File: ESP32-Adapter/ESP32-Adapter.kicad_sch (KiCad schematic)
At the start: 0 parts

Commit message: complete adapter board schem
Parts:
- added C1: 0.1µ, symbol Device:C
- added C2: 1µ, symbol Device:C
- added D1: D, symbol Device:D
- added J1, J4, J5, J6, J7, J8, J9: Conn_01x01_Socket, symbol Connector:Conn_01x01_Socket
- added J12, J13: Conn_01x05, symbol Connector_Generic:Conn_01x05
- added J14: Conn_01x04, symbol Connector_Generic:Conn_01x04
- added J2, J3: Conn_01x03, symbol Connector_Generic:Conn_01x03
- added R1: 820, symbol Device:R
- added R2: 270, symbol Device:R
- added U1: ESP32-C5-DevKitC-1, PCM_Espressif:ESP32-C5-DevKitC-1, symbol PCM_Espressif:ESP32-C5-DevKitC-1
- added U2: LM317_TO-263, Package_TO_SOT_SMD:TO-263-2, symbol Regulator_Linear:LM317_TO-263
- added U3: Adafruit CANPAL, symbol Interface_CAN_LIN:CANPAL
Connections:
- new net: J3.1 (Pin_1), J5.1 (Pin_1)
- new net: J14.2 (Pin_2), U1.11 (GPIO7)
- new net: J14.3 (Pin_3), U1.10 (GPIO6)
- new net: J14.4 (Pin_4), J6.1 (Pin_1), J8.1 (Pin_1), U1.1 (3V3)
- new net: C2.1, D1.2 (A), U2.2 (VO)
- new net: C1.1, J1.1 (Pin_1), R2.2, U2.3 (VI)
- new net: J12.1 (Pin_1), U1.4 (GPIO3/MTDI)
- new net: J12.2 (Pin_2), U1.28 (GPIO23)
- new net: J12.3 (Pin_3), U1.25 (GPIO9)
- new net: D1.1 (K), J12.5 (Pin_5), J13.5 (Pin_5), J7.1 (Pin_1), J9.1 (Pin_1), U1.14 (5V), U3. (CANL)
- new net: J3.2 (Pin_2), U1.3 (GPIO2/MTMS)
- new net: R1.2, U2.1 (ADJ)
- new net: J13.1 (Pin_1), U1.29 (GPIO24)
- new net: J13.2 (Pin_2), U1.26 (GPIO10)
- new net: J13.3 (Pin_3), U1.24 (GPIO8)
- new net: U1.5 (GPIO4/MTCK), U3. (CANL)
- new net: U1.6 (GPIO5/MTDO), U3. (CANL)
- new net: J2.2 (Pin_2), U1.8 (GPIO1)
- new net: J2.1 (Pin_1), J4.1 (Pin_1)
- new net GND: C1.2, C2.2, J12.4 (Pin_4), J13.4 (Pin_4), J14.1 (Pin_1), J2.3 (Pin_3), J3.3 (Pin_3), R1.1, R2.1, U1.15 (GND), U1.18 (GND), U1.21 (GND), U1.32 (GND), U3. (CANL)
- no-connect marks 0 -> 13
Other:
- note added: "3.3V"
- note added: "5V"
- note added: "A1"
- note added: "A2"
- note added: "Analog 1"
- note added: "Analog 2"
- note added: "B1"
- note added: "B2"
- note added: "CAN RX"
- note added: "CAN TX"
- note added: "Encoder 1"
- note added: "Encoder 2"
- note added: "GND"
- note added: "I2C"
- note added: "IDX1"
- note added: "IDX2"
- note added: "MILLIONS NERVES"
- note added: "SCL"
- note added: "SDA"
- note added: "SIG1"
- note added: "SIG2"
- note added: "V-in from PDP"
- note added: "Vcc"
- note added: "vash the stampede"

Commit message: create pcb
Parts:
- removed J1, J4, J5, J6, J7, J8, J9: Conn_01x01_Socket, symbol Connector:Conn_01x01_Socket
- added J1: Conn_01x08_Pin, Connector_PinHeader_2.54mm:PinHeader_2x04_P2.54mm_Vertical, symbol Connector:Conn_01x08_Pin
- added J10: Barrel_Jack, Connector_BarrelJack:BarrelJack_CUI_PJ-063AH_Horizontal, symbol Connector:Barrel_Jack
- C1, C2: footprint (none) -> Capacitor_SMD:C_0402_1005Metric
- D1: footprint (none) -> Diode_SMD:D_0805_2012Metric
- J12, J13: footprint (none) -> Connector_JST:JST_XH_S5B-XH-A-1_1x05_P2.50mm_Horizontal
- J14: footprint (none) -> Connector_JST:JST_XH_S4B-XH-A-1_1x04_P2.50mm_Horizontal
- J2, J3: footprint (none) -> Connector_JST:JST_XH_S3B-XH-A-1_1x03_P2.50mm_Horizontal
- R1, R2: footprint (none) -> Resistor_SMD:R_0402_1005Metric
- U3: footprint (none) -> Audio_Module:canpal
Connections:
- net GND: now also J12.1 (Pin_1), J13.1 (Pin_1), J14.4 (Pin_4), U3.2 (GND), J10.2; no longer J12.4 (Pin_4), J13.4 (Pin_4), J14.1 (Pin_1), R2.1, U3. (CANL)
- net at J3.1 (Pin_1): now also J1.6 (Pin_6), J1.8 (Pin_8)
- net I2C SCL: now reaches J14.2 (Pin_2), U1.11 (GPIO7)
- net I2C SDA: now reaches J14.3 (Pin_3), U1.10 (GPIO6)
- net +3.3V: now reaches U1.1 (3V3)
- net +3.3V: now also J14.1 (Pin_1), U3.1 (Vcc), J1.3 (Pin_3), J1.7 (Pin_7); no longer J14.4 (Pin_4)
- net at C2.1, D1.2 (A), U2.2 (VO): now also R2.2
- net at C1.1, U2.3 (VI): now also J10.1; no longer R2.2
- net B2: now reaches U1.4 (GPIO3/MTDI)
- net B2: now also J12.2 (Pin_2); no longer J12.1 (Pin_1)
- net A2: now reaches U1.28 (GPIO23)
- net A2: now also J12.3 (Pin_3); no longer J12.2 (Pin_2)
- net IDX2: now reaches U1.25 (GPIO9)
- net IDX2: now also J12.4 (Pin_4); no longer J12.3 (Pin_3)
- net +5V: now reaches D1.1 (K), J12.5 (Pin_5), J13.5 (Pin_5), U1.14 (5V)
- net +5V: now also J1.1 (Pin_1), J1.5 (Pin_5); no longer U3. (CANL)
- net SIG2: now reaches J3.2 (Pin_2), U1.3 (GPIO2/MTMS)
- net at R1.2, U2.1 (ADJ): now also R2.1
- net B1: now reaches U1.29 (GPIO24)
- net B1: now also J13.2 (Pin_2); no longer J13.1 (Pin_1)
- net A1: now reaches U1.26 (GPIO10)
- net A1: now also J13.3 (Pin_3); no longer J13.2 (Pin_2)
- net IDX1: now reaches U1.24 (GPIO8)
- net IDX1: now also J13.4 (Pin_4); no longer J13.3 (Pin_3)
- net CAN TX: now reaches U1.5 (GPIO4/MTCK)
- net CAN TX: now also U3.4 (TX); no longer U3. (CANL)
- net CAN RX: now reaches U1.6 (GPIO5/MTDO)
- net CAN RX: now also U3.3 (RX); no longer U3. (CANL)
- net SIG1: now reaches J2.2 (Pin_2), U1.8 (GPIO1)
- net at J2.1 (Pin_1): now also J1.2 (Pin_2), J1.4 (Pin_4)
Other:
- note added: "Analog"
- note added: "CANPal"
- note added: "PDP Step-Down"
- note added: "PDP-V"
- note added: "Quadrature Encoders"
- note added: "Voltage Sel"
- note removed: "3.3V"
- note removed: "5V"
- note removed: "A1"
- note removed: "A2"
- note removed: "B1"
- note removed: "B2"
- note removed: "CAN RX"
- note removed: "CAN TX"
- note removed: "GND"
- note removed: "IDX1"
- note removed: "IDX2"
- note removed: "SCL"
- note removed: "SDA"
- note removed: "SIG1"
- note removed: "SIG2"
- note removed: "V-in from PDP"
- moved on the sheet: C1, C2, D1, J12, J13, J14, J2, J3, R1, R2, U2

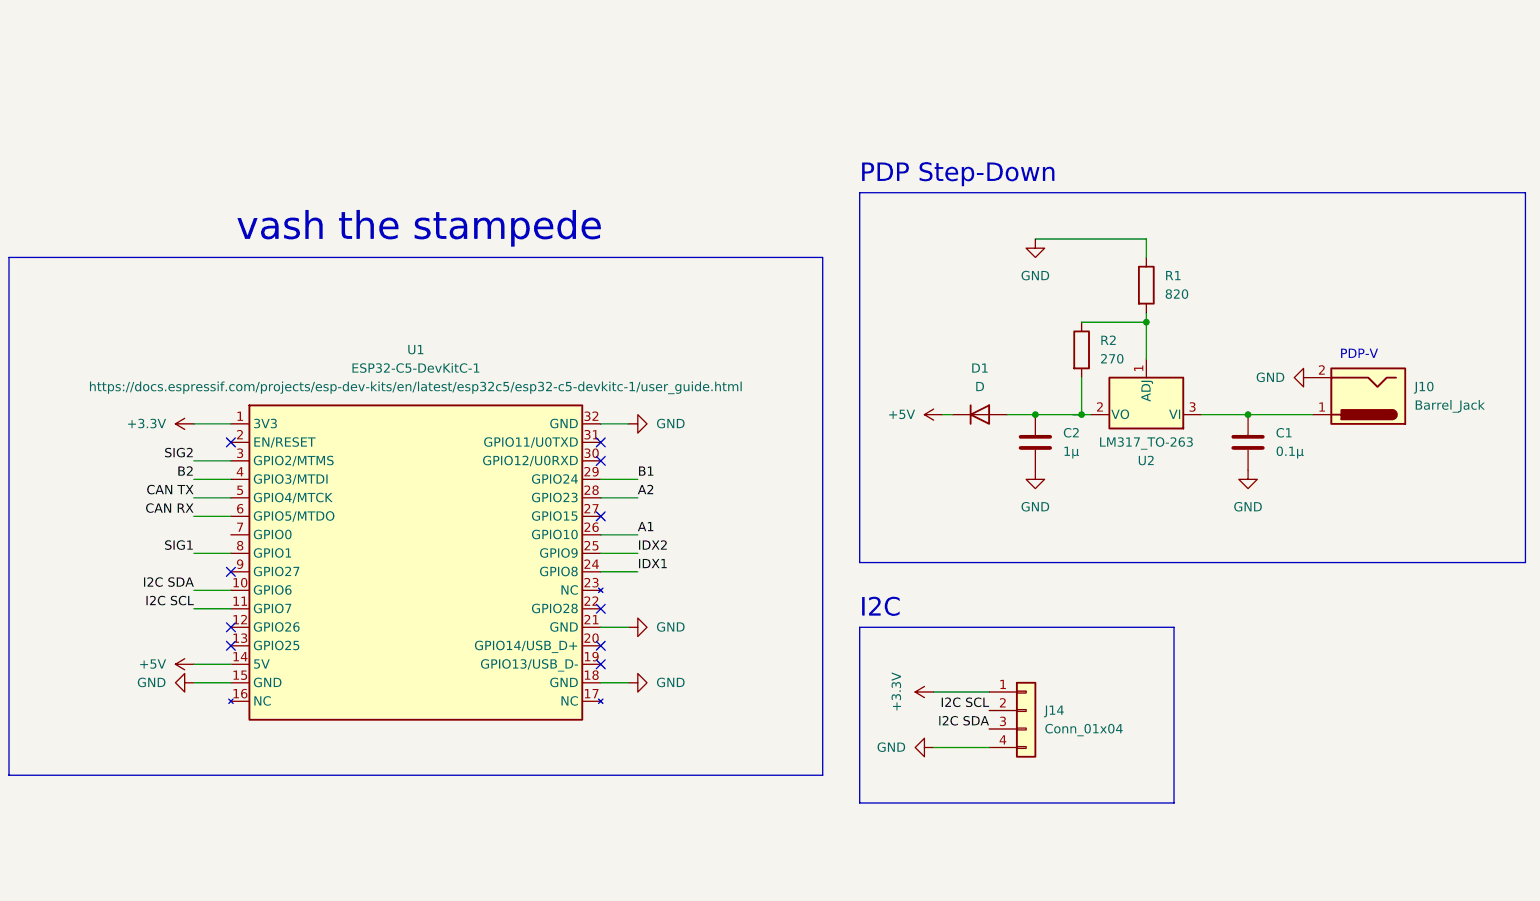
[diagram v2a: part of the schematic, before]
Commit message: finish first version of neopixel board
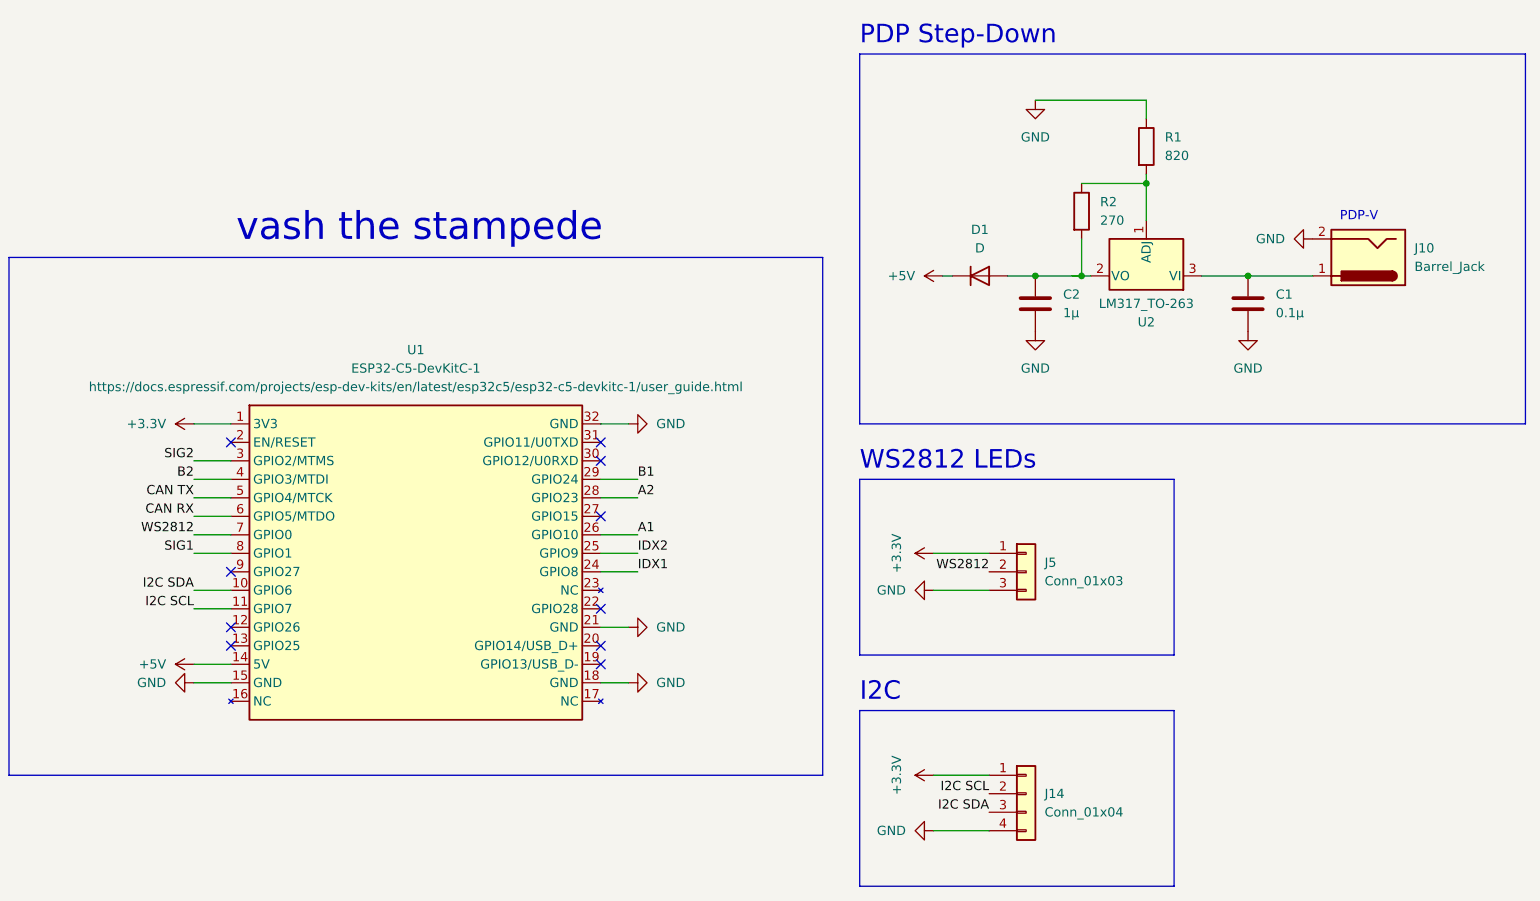
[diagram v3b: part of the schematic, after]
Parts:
- added J5: Conn_01x03, Connector_JST:JST_XH_S3B-XH-A-1_1x03_P2.50mm_Horizontal, symbol Connector_Generic:Conn_01x03
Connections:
- net +3.3V: now also J5.1 (Pin_1)
- net GND: now also J5.3 (Pin_3)
- net WS2812: now reaches U1.7 (GPIO0)
- net WS2812: now also J5.2 (Pin_2)
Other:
- note added: "WS2812 LEDs"
- moved on the sheet: C1, C2, D1, J10, J14, R1, R2, U2

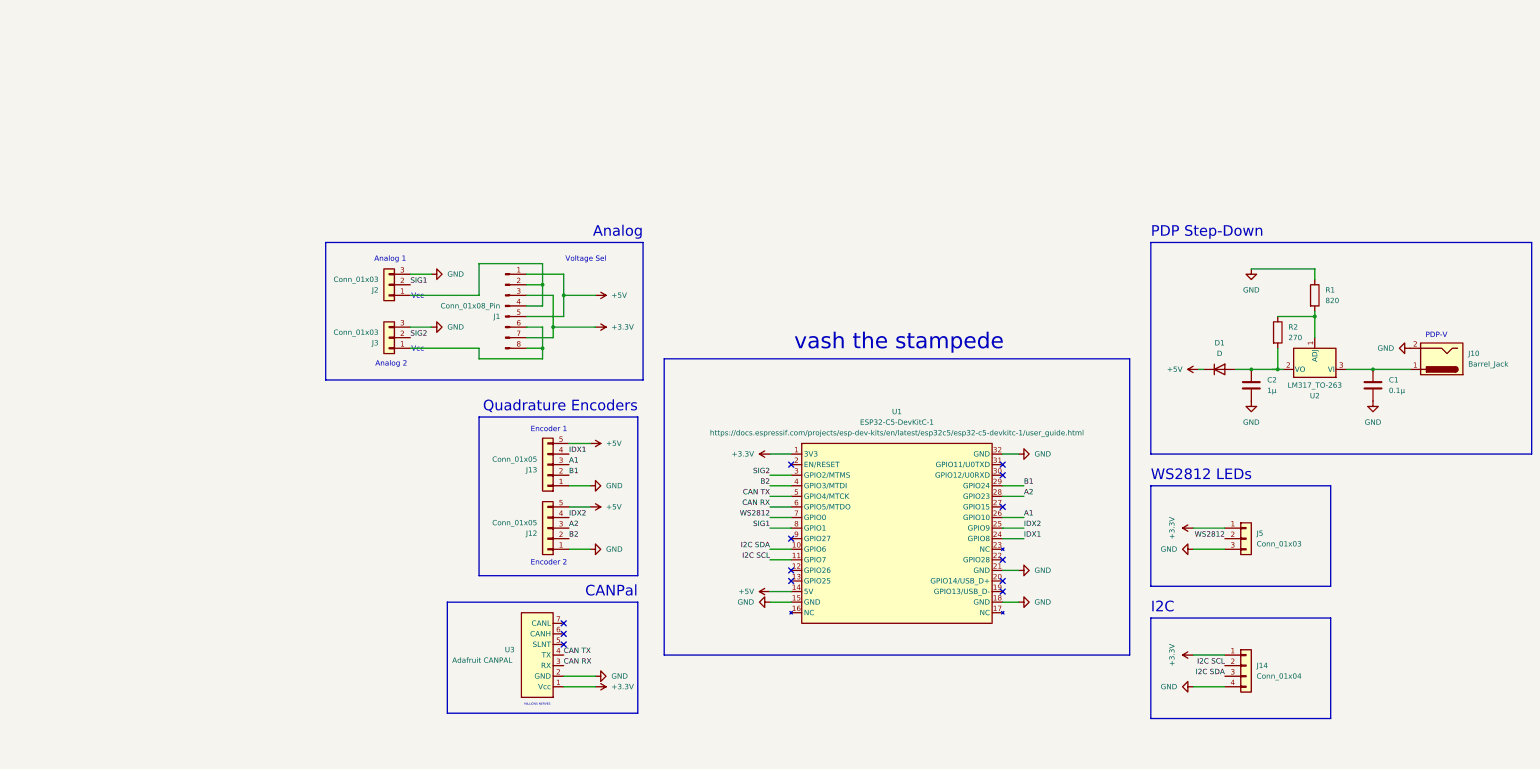
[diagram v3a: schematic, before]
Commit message: Redo board partially
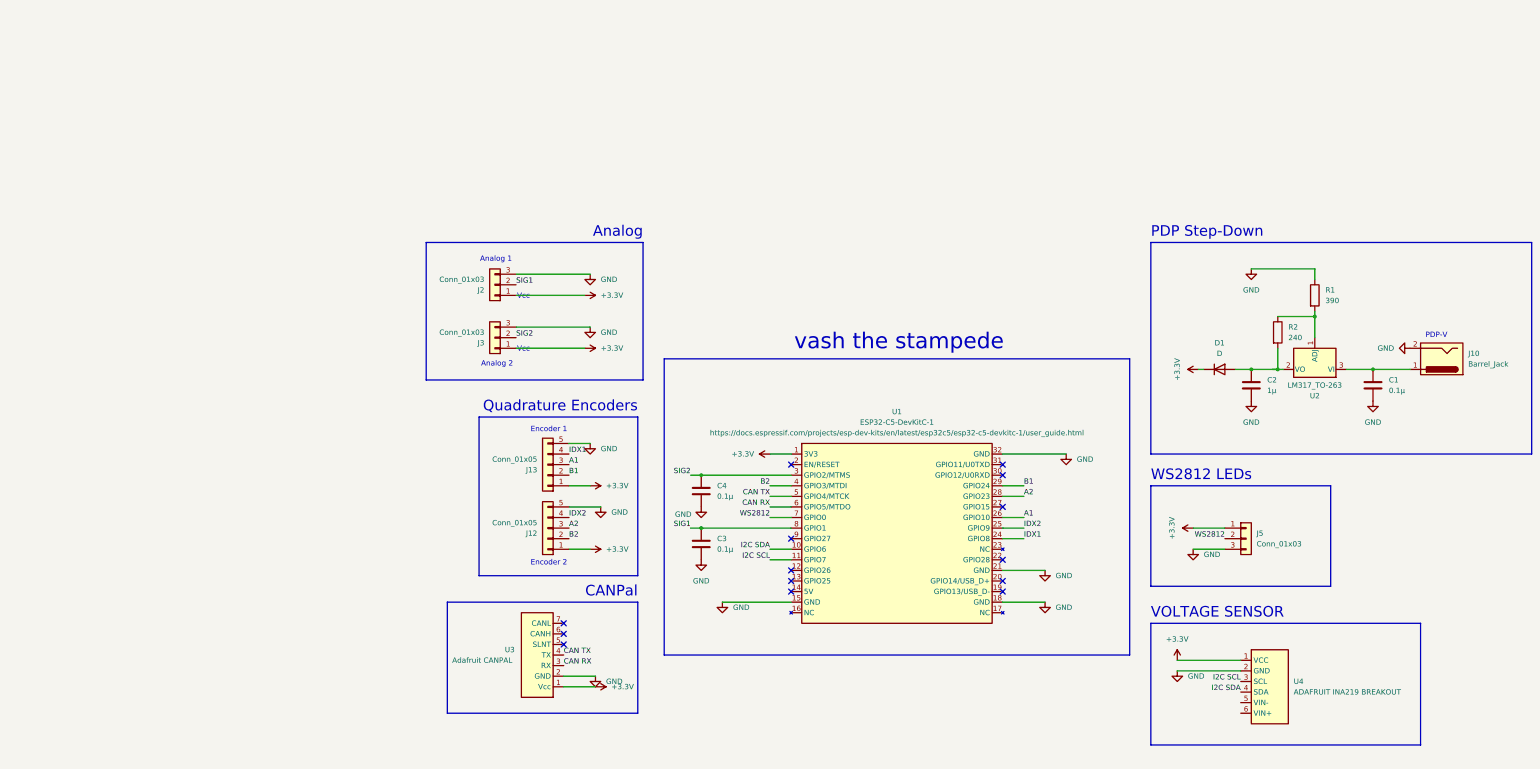
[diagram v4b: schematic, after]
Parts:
- removed J1: Conn_01x08_Pin, Connector_PinHeader_2.54mm:PinHeader_2x04_P2.54mm_Vertical, symbol Connector:Conn_01x08_Pin
- removed J14: Conn_01x04, Connector_JST:JST_XH_S4B-XH-A-1_1x04_P2.50mm_Horizontal, symbol Connector_Generic:Conn_01x04
- added C3, C4: 0.1µ, Capacitor_SMD:C_0402_1005Metric, symbol Device:C
- added U4: ADAFRUIT INA219 BREAKOUT, Audio_Module:INA219 Breakout, symbol Analog_ADC:INA219_ADAFRUIT
- R1: value 820 -> 390
- R2: value 270 -> 240
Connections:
- net +3.3V: now also D1.1 (K), J12.1 (Pin_1), J13.1 (Pin_1), J2.1 (Pin_1), J3.1 (Pin_1), U4.1 (VCC)
- net GND: now also J12.5 (Pin_5), J13.5 (Pin_5), C3.2, C4.2, U4.2 (GND); no longer J12.1 (Pin_1), J13.1 (Pin_1)
- net I2C SCL: now also U4.3 (SCL)
- net I2C SDA: now also U4.4 (SDA)
- net SIG1: now also C3.1
- net SIG2: now also C4.1
- removed net +5V: D1.1 (K), J12.5 (Pin_5), J13.5 (Pin_5), U1.14 (5V)
- no-connect marks 13 -> 14
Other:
- note added: "VOLTAGE SENSOR"
- note removed: "I2C"
- note removed: "MILLIONS NERVES"
- note removed: "Voltage Sel"
- moved on the sheet: J2, J3
